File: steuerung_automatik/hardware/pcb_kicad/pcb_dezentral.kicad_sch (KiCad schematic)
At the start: 57 parts, among them J1 weidmueller_SL5.08HC-06-90, J2 weidmueller_SL5.08HC-10-90, Q1 AO3400A, SW1 dip_switch_SPST16, U1 SP3485EN-L/TR, U2 AOZ1282CI

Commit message: pcb_dezentral v0.8
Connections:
- net +3V3: now also R15.1
- net GND: now also R16.2; no longer R15.1, R16.1
- net MODBUS_DE: now also D17.2 (A)
- net MODBUS_RO: now also D27.1 (K)
- net at R15.2: now also D27.2 (A); no longer D17.1 (K)
- removed net modbus_led: D17.2 (A), D27.1 (K)
- new net: D17.1 (K), R16.1
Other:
- note removed: "Modbus LED"
- moved on the sheet: R14, R15

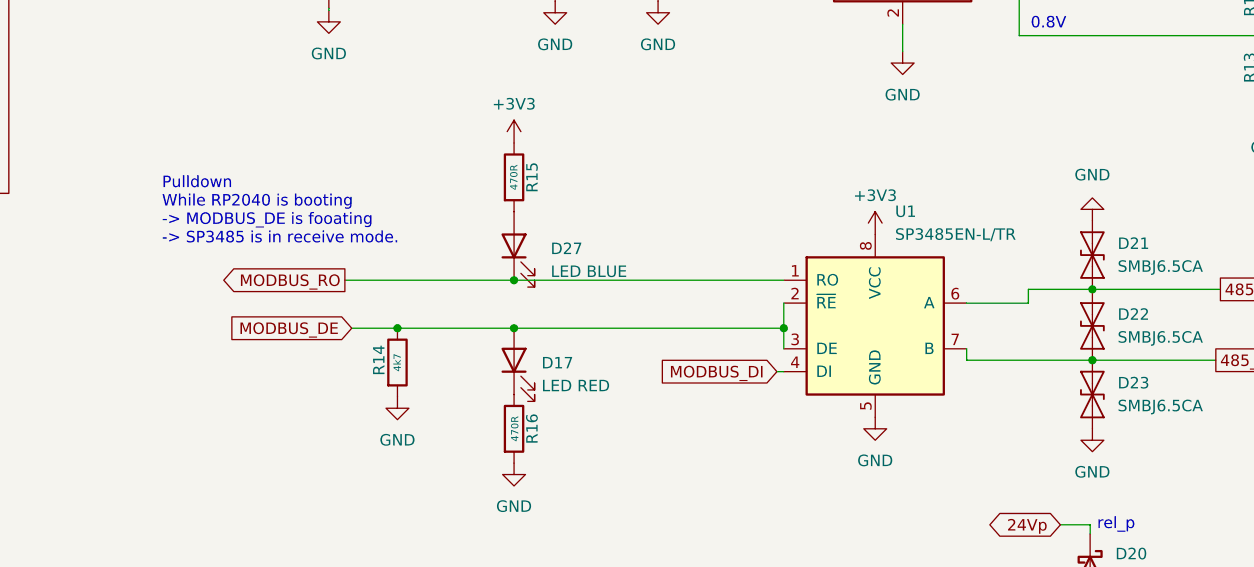
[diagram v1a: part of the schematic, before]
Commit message: pcb_dezentral, update J1/J2, v0.8
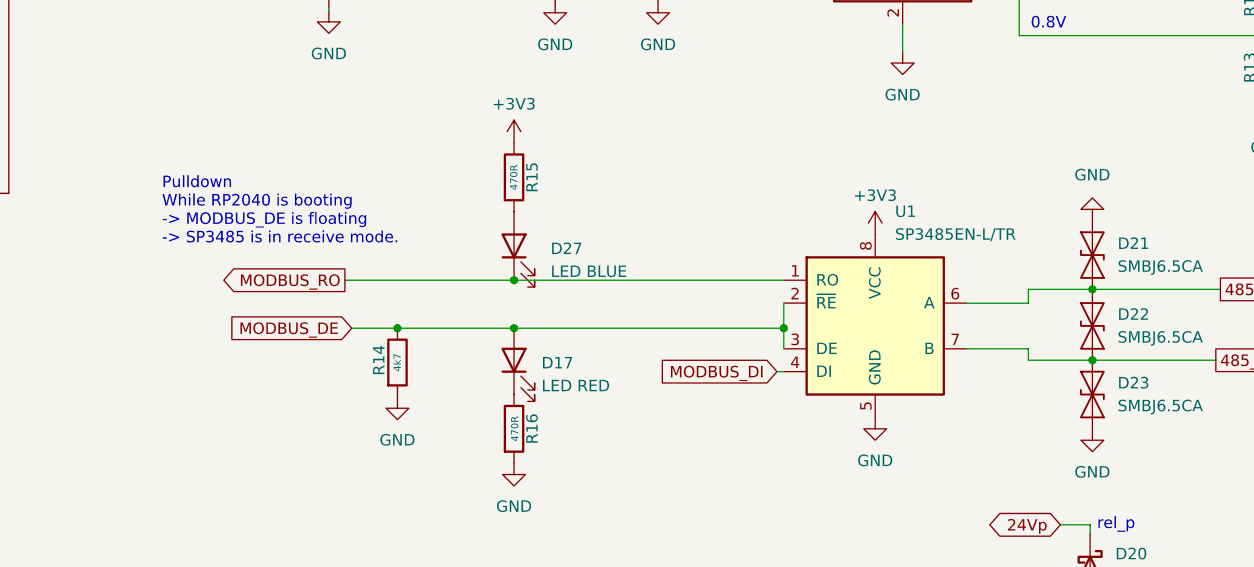
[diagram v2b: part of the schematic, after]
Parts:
- C1: JLC C49678 -> C515689
- J1: JLC (none) -> C8472
- J2: JLC (none) -> C46026
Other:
- note added: "Pulldown While RP2040 is booting -> MODBUS_DE is floating -> SP3485 is in receive mode."
- note removed: "Pulldown While RP2040 is booting -> MODBUS_DE is fooating -> SP3485 is in receive mode."
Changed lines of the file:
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@@
+    (stroke (width 0) (type default))
+  )
+  (wire (pts (xy 179.578 77.978) (xy 172.72 77.978))
     (stroke (width 0) (type default))
   )
@@
     (stroke (width 0) (type default))
   )
-  (wire (pts (xy 172.72 79.248) (xy 186.69 79.248))
+  (wire (pts (xy 179.578 79.248) (xy 186.69 79.248))
     (stroke (width 0) (type default))
   )
@@
     (stroke (width 0) (type default))
   )
-  (wire (pts (xy 172.72 77.978) (xy 172.72 79.248))
+  (wire (pts (xy 179.578 77.978) (xy 179.578 79.248))
     (stroke (width 0) (type default))
   )
@@
     (effects (font (size 1.27 1.27)) (justify left bottom))
   )
-  (text "Pulldown\nWhile RP2040 is booting\n-> MODBUS_DE is fooating\n-> SP3485 is in receive mode."
+  (text "Pulldown\nWhile RP2040 is booting\n-> MODBUS_DE is floating\n-> SP3485 is in receive mode."
     (at 83.312 66.548 0)
     (effects (font (size 1.27 1.27)) (justify left bottom))
@@
       (effects (font (size 1.27 1.27)) hide)
     )
-    (property "JLC" "C49678" (at 127 35.56 0)
+    (property "JLC" "C515689" (at 127 35.56 0)
       (effects (font (size 1.27 1.27)) hide)
     )
@@
     (property "Arrow Price/Stock" "" (at 252.73 1131.064 0)
       (effects (font (size 1.27 1.27)) (justify left top) hide)
+    )
+    (property "JLC" "C46026" (at 236.22 136.144 0)
+      (effects (font (size 1.27 1.27)) hide)
     )
     (pin "1")
@@
       (effects (font (size 1.27 1.27)) (justify left top) hide)
     )
-    (pin "1")
+    (property "JLC" "C8472" (at 236.474 71.374 0)
+      (effects (font (size 1.27 1.27)) hide)
+    )
+    (pin "1")
